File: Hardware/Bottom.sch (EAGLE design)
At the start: 109 parts, among them IC1 OP491SOIC_N14, IC2 74AC74D, IC3 74LVC1G17DCK, IC4 LT6231, IC5 SN74CBT3253SOIC16, Q1 DMPH6050SK3, Q2 25MHz

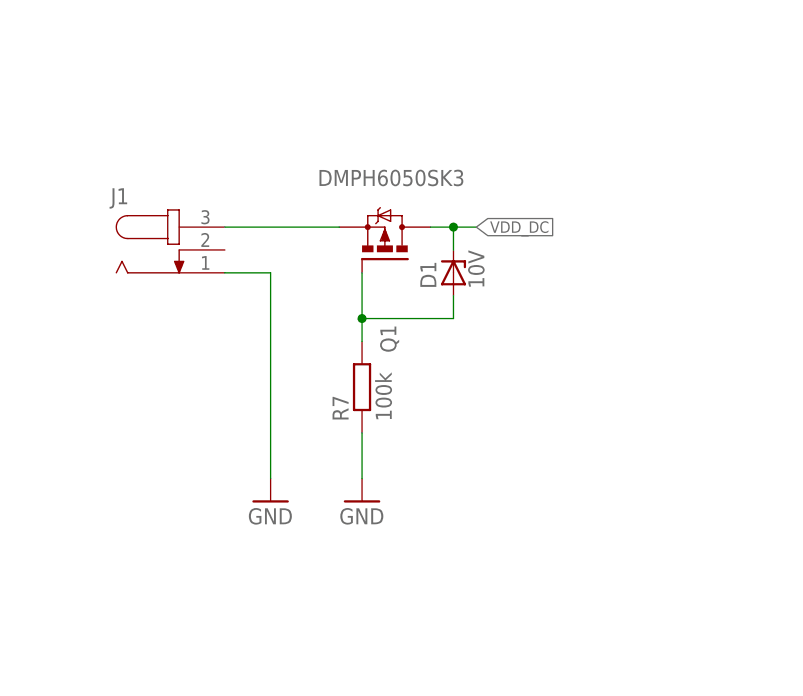
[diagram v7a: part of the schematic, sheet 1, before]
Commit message: Advance layout bottom
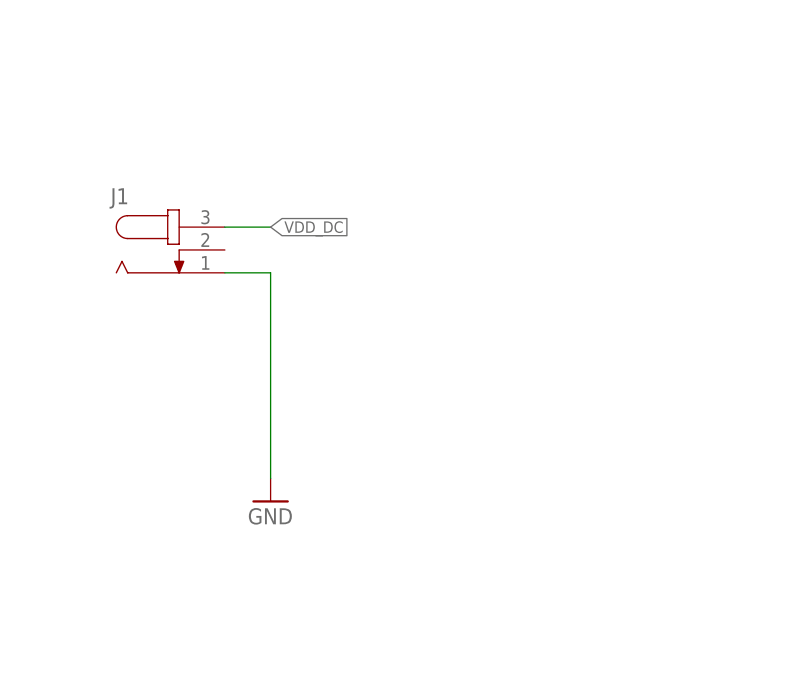
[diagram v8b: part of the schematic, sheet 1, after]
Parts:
- removed D1: 10V, diode:ZENER-DIODESOT23
- removed Q1: DMPH6050SK3, MyLib:DMP3099L
- removed R7: 100k, rcl:R-EU_R0402
- removed R8: 10k, rcl:R-EU_R0603
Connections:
- removed net N$12: J1.3, Q1.S
- removed net N$9: D1.A, Q1.G, R7.2
- removed net SPI_ADC_MISO: R8.1, U$7.SDO
- net GND: no longer R7.1
- net SPI_MCS_MISO: now also U$7.SDO; no longer R8.2
- net VDD_DC: now also J1.3; no longer D1.C, Q1.D
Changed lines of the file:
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@@
 <part name="R5" library="rcl" library_urn="urn:adsk.eagle:library:334" deviceset="R-EU_" device="R0402" package3d_urn="urn:adsk.eagle:package:23547/2" value="10k"/>
 <part name="R6" library="rcl" library_urn="urn:adsk.eagle:library:334" deviceset="R-EU_" device="R0402" package3d_urn="urn:adsk.eagle:package:23547/2" value="10k"/>
-<part name="Q1" library="MyLib" deviceset="DMP3099L" device="" package3d_urn="urn:adsk.eagle:package:28738/2" value="DMPH6050SK3"/>
-<part name="D1" library="diode" library_urn="urn:adsk.eagle:library:210" deviceset="ZENER-DIODE" device="SOT23" package3d_urn="urn:adsk.eagle:package:43389/2" value="10V"/>
-<part name="R7" library="rcl" library_urn="urn:adsk.eagle:library:334" deviceset="R-EU_" device="R0402" package3d_urn="urn:adsk.eagle:package:23547/2" value="100k"/>
-<part name="GND20" library="supply1" library_urn="urn:adsk.eagle:library:371" deviceset="GND" device=""/>
 <part name="GND21" library="supply1" library_urn="urn:adsk.eagle:library:371" deviceset="GND" device=""/>
 <part name="C19" library="rcl" library_urn="urn:adsk.eagle:library:334" deviceset="C-EU" device="C0603" package3d_urn="urn:adsk.eagle:package:23616/2" value="100n"/>
@@
 <part name="GND43" library="supply1" library_urn="urn:adsk.eagle:library:371" deviceset="GND" device=""/>
 <part name="GND44" library="supply1" library_urn="urn:adsk.eagle:library:371" deviceset="GND" device=""/>
-<part name="R8" library="rcl" library_urn="urn:adsk.eagle:library:334" deviceset="R-EU_" device="R0603" package3d_urn="urn:adsk.eagle:package:23555/2" value="10k"/>
 <part name="C26" library="rcl" library_urn="urn:adsk.eagle:library:334" deviceset="C-EU" device="C0603" package3d_urn="urn:adsk.eagle:package:23616/2" value="100n"/>
 <part name="GND45" library="supply1" library_urn="urn:adsk.eagle:library:371" deviceset="GND" device=""/>
@@
 <attribute name="VALUE" x="20.32" y="157.48" size="1.778" layer="96"/>
 </instance>
-<instance part="Q1" gate="G$1" x="50.8" y="162.56" smashed="yes" rot="R90">
-<attribute name="VALUE" x="59.69" y="171.45" size="1.778" layer="96" rot="R180"/>
-<attribute name="NAME" x="52.07" y="151.13" size="1.778" layer="95" rot="R90"/>
-</instance>
-<instance part="D1" gate="G$1" x="58.42" y="160.02" smashed="yes" rot="R90">
-<attribute name="NAME" x="56.515" y="158.242" size="1.778" layer="95" rot="R90"/>
-<attribute name="VALUE" x="61.849" y="158.242" size="1.778" layer="96" rot="R90"/>
-</instance>
-<instance part="R7" gate="G$1" x="48.26" y="147.32" smashed="yes" rot="R90">
-<attribute name="NAME" x="46.7614" y="143.51" size="1.778" layer="95" rot="R90"/>
-<attribute name="VALUE" x="51.562" y="143.51" size="1.778" layer="96" rot="R90"/>
-</instance>
-<instance part="GND20" gate="1" x="48.26" y="134.62" smashed="yes">
-<attribute name="VALUE" x="45.72" y="132.08" size="1.778" layer="96"/>
-</instance>
 <instance part="GND21" gate="1" x="38.1" y="134.62" smashed="yes">
 <attribute name="VALUE" x="35.56" y="132.08" size="1.778" layer="96"/>
@@
 <pinref part="GND19" gate="1" pin="GND"/>
 <wire x1="203.2" y1="96.52" x2="203.2" y2="91.44" width="0.1524" layer="91"/>
-</segment>
-<segment>
-<pinref part="R7" gate="G$1" pin="1"/>
-<pinref part="GND20" gate="1" pin="GND"/>
-<wire x1="48.26" y1="137.16" x2="48.26" y2="142.24" width="0.1524" layer="91"/>
 </segment>
 <segment>
@@
 </segment>
 <segment>
-<pinref part="Q1" gate="G$1" pin="D"/>
-<wire x1="55.88" y1="165.1" x2="58.42" y2="165.1" width="0.1524" layer="91"/>
-<pinref part="D1" gate="G$1" pin="C"/>
-<wire x1="58.42" y1="165.1" x2="60.96" y2="165.1" width="0.1524" layer="91"/>
-<wire x1="58.42" y1="162.56" x2="58.42" y2="165.1" width="0.1524" layer="91"/>
-<junction x="58.42" y="165.1"/>
-<label x="60.96" y="165.1" size="1.27" layer="95" xref="yes"/>
-</segment>
-</net>
-<net name="N$9" class="0">
-<segment>
-<pinref part="D1" gate="G$1" pin="A"/>
-<wire x1="58.42" y1="157.48" x2="58.42" y2="154.94" width="0.1524" layer="91"/>
-<wire x1="58.42" y1="154.94" x2="48.26" y2="154.94" width="0.1524" layer="91"/>
-<pinref part="R7" gate="G$1" pin="2"/>
-<wire x1="48.26" y1="154.94" x2="48.26" y2="152.4" width="0.1524" layer="91"/>
-<pinref part="Q1" gate="G$1" pin="G"/>
-<wire x1="48.26" y1="154.94" x2="48.26" y2="160.02" width="0.1524" layer="91"/>
-<junction x="48.26" y="154.94"/>
-</segment>
-</net>
-<net name="N$12" class="0">
-<segment>
+<wire x1="33.02" y1="165.1" x2="38.1" y2="165.1" width="0.1524" layer="91"/>
+<label x="38.1" y="165.1" size="1.27" layer="95" xref="yes"/>
 <pinref part="J1" gate="G$1" pin="3"/>
-<pinref part="Q1" gate="G$1" pin="S"/>
-<wire x1="33.02" y1="165.1" x2="45.72" y2="165.1" width="0.1524" layer="91"/>
 </segment>
 </net>
@@
 <instance part="GND44" gate="1" x="228.6" y="10.16" smashed="yes">
 <attribute name="VALUE" x="226.06" y="7.62" size="1.778" layer="96"/>
-</instance>
-<instance part="R8" gate="G$1" x="101.6" y="38.1" smashed="yes" rot="R180">
-<attribute name="NAME" x="105.41" y="36.6014" size="1.778" layer="95" rot="R180"/>
-<attribute name="VALUE" x="105.41" y="41.402" size="1.778" layer="96" rot="R180"/>
 </instance>
 <instance part="C26" gate="G$1" x="312.42" y="241.3" smashed="yes">
@@
 <segment>
 <pinref part="SV4" gate="G$1" pin="5"/>
-<pinref part="R8" gate="G$1" pin="2"/>
 <wire x1="96.52" y1="38.1" x2="93.98" y2="38.1" width="0.1524" layer="91"/>
+<wire x1="96.52" y1="38.1" x2="109.22" y2="38.1" width="0.1524" layer="91"/>
+<label x="109.22" y="38.1" size="1.27" layer="95" xref="yes"/>
+</segment>
+<segment>
+<pinref part="U$7" gate="G$1" pin="SDO"/>
+<wire x1="246.38" y1="27.94" x2="248.92" y2="27.94" width="0.1524" layer="91"/>
+<label x="246.38" y="27.94" size="1.27" layer="95" rot="R180" xref="yes"/>
 </segment>
 </net>
@@
 </segment>
 </net>
-<net name="SPI_ADC_MISO" class="0">
-<segment>
-<pinref part="R8" gate="G$1" pin="1"/>
-<wire x1="106.68" y1="38.1" x2="109.22" y2="38.1" width="0.1524" layer="91"/>
-<label x="109.22" y="38.1" size="1.27" layer="95" xref="yes"/>
-</segment>
-<segment>
-<pinref part="U$7" gate="G$1" pin="SDO"/>
-<wire x1="246.38" y1="27.94" x2="248.92" y2="27.94" width="0.1524" layer="91"/>
-<label x="246.38" y="27.94" size="1.27" layer="95" rot="R180" xref="yes"/>
-</segment>
-</net>
